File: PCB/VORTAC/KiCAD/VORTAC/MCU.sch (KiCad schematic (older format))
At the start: 1 part

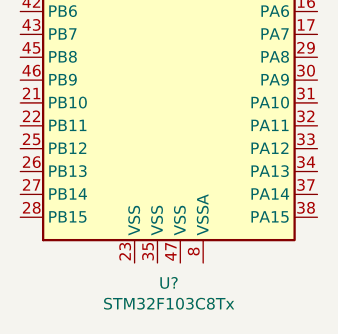
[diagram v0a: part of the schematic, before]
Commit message: pcb, step and headers
-headers schematic updated
-created rough pcb placement of headers
-created step file for inspection in fusion 360
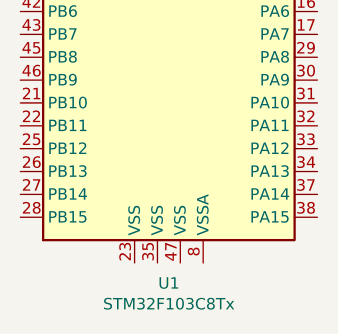
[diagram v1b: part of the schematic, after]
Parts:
- gave numbers to parts that had none: 1
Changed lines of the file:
@@
 $EndDescr
 $Comp
-L MCU_ST_STM32F1:STM32F103C8Tx U?
+L MCU_ST_STM32F1:STM32F103C8Tx U1
 U 1 1 6140AA25
 P 3450 3900
-F 0 "U?" H 3400 2311 50  0000 C CNN
+F 0 "U1" H 3400 2311 50  0000 C CNN
 F 1 "STM32F103C8Tx" H 3400 2220 50  0000 C CNN
 F 2 "Package_QFP:LQFP-48_7x7mm_P0.5mm" H 2850 2500 50  0001 R CNN

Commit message: Schematic and Lib Updates
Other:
- moved on the sheet: U1
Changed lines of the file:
@@
 L MCU_ST_STM32F1:STM32F103C8Tx U1
 U 1 1 6140AA25
-P 3450 3900
-F 0 "U1" H 3400 2311 50  0000 C CNN
-F 1 "STM32F103C8Tx" H 3400 2220 50  0000 C CNN
-F 2 "Package_QFP:LQFP-48_7x7mm_P0.5mm" H 2850 2500 50  0001 R CNN
-F 3 "http://www.st.com/st-web-ui/static/active/en/resource/technical/document/datasheet/CD00161566.pdf" H 3450 3900 50  0001 C CNN
-	1    3450 3900
+P 3500 3550
+F 0 "U1" H 3450 1961 50  0000 C CNN
+F 1 "STM32F103C8Tx" H 3450 1870 50  0000 C CNN
+F 2 "Package_QFP:LQFP-48_7x7mm_P0.5mm" H 2900 2150 50  0001 R CNN
+F 3 "http://www.st.com/st-web-ui/static/active/en/resource/technical/document/datasheet/CD00161566.pdf" H 3500 3550 50  0001 C CNN
+	1    3500 3550
 	1    0    0    -1
 $EndComp

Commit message: pushie
updates and stuff
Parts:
- added 10uH1, 10uH2: L, Inductor_SMD:L_Sunlord_MWSA0518_5.4x5.2mm, symbol Device:L
- added C11, C12: 10uF, Capacitor_SMD:C_1206_3216Metric, symbol Device:C_Small
- added C13, C14, C15, C17: 0.1uF, Capacitor_SMD:C_0603_1608Metric, symbol Device:C_Small
- added C16: 360pF, Capacitor_SMD:C_0603_1608Metric, symbol Device:C_Small
- added C18: 3.3nF, Capacitor_SMD:C_0603_1608Metric, symbol Device:C_Small
- added C19: 30pF, Capacitor_SMD:C_0603_1608Metric, symbol Device:C_Small
- added C20: 56pF, Capacitor_SMD:C_0603_1608Metric, symbol Device:C_Small
- added C21, C23, C25: 47uF, Capacitor_SMD:C_1206_3216Metric, symbol Device:C_Small
- added C22, C24, C26: 47uF, Capacitor_SMD:C_0805_2012Metric, symbol Device:C_Small
- added C? (x2): 1uF, Capacitor_SMD:C_0603_1608Metric, symbol Device:C_Small
- added R28: 36.5k, Resistor_SMD:R_0402_1005Metric, symbol Device:R_Small
- added R29: 10k, Resistor_SMD:R_0402_1005Metric, symbol Device:R_Small
- added R30, R31: 95k, Resistor_SMD:R_0402_1005Metric, symbol Device:R_Small
- added R32, R34: 100k, Resistor_SMD:R_0402_1005Metric, symbol Device:R_Small
- added R33: 7.15k, Resistor_SMD:R_0402_1005Metric, symbol Device:R_Small
- added R35: 19.1k, Resistor_SMD:R_0402_1005Metric, symbol Device:R_Small
- added U3, U4: TPS54335ADRCR, Package_SON:VSON-10-1EP_3x3mm_P0.5mm_EP1.65x2.4mm_ThermalVias, symbol ToolChanger:TPS54335ADRCR
- added U?: TLV73333PDBV, Package_TO_SOT_SMD:SOT-23-5, symbol Regulator_Linear:TLV73333PDBV
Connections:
- new net: R30.2, U3.10 (RT)
- new net: 10uH1.1, C15.1, U3.2 (PH)
- new net: R32.2, R33.1, U3.6 (VSENSE)
- new net: C16.1, R28.2, U3.7 (COMP)
- new net: C15.2, U3.9 (BOOT)
- new net: C19.1, R28.1
- new net: R31.2, U4.10 (RT)
- new net: 10uH2.1, C17.1, U4.2 (PH)
- new net: C17.2, U4.9 (BOOT)
- new net: C20.1, R29.1
- new net: C18.1, R29.2, U4.7 (COMP)
- new net: R34.2, R35.1, U4.6 (VSENSE)
- new net 12V: 10uH1.2, C21.1, C23.1, C25.1, R32.1
- new net 3.3V: C?.1, U?.5 (OUT)
- new net 5V: 10uH2.2, C22.1, C24.1, C26.1, C?.1, R34.1, U?.1 (IN), U?.3 (EN)
- new net GND: C11.2, C12.2, C13.2, C14.2, C16.2, C18.2, C19.2, C20.2, C21.2, C22.2, C23.2, C24.2, C25.2, C26.2, C?.2, C?.2, R30.1, R31.1, R33.2, R35.2, U3.11 (THRM), U3.3 (GND), U3.4 (GND), U3.5 (GND), U4.11 (THRM), U4.3 (GND), U4.4 (GND), U4.5 (GND), U?.2 (GND)
- new net V_IN: C11.1, C12.1, C13.1, C14.1, U3.1 (VIN), U4.1 (VIN)
- no-connect marks 0 -> 2
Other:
- note added: "12V DC-DC Converter\n(capable of min 2A)"
- note added: "5V DC-DC Converter\n(capable of min 2.5A)"
- note added: "R2 = 0.8 / (VOUT-0.8) * 100K\nR2 = 19.047 >> 19.1K\n\nVOUT = 0.8 * R1/R2 + 0.8\nVOUT = 4.98V\n\nRT = 55300/FSW^-1.025\nRT(500 kHz) = 94.68K"
- note added: "R2 = 0.8 / (VOUT-0.8) * 100K\nR2 = 7.142 >> 7.15K\n\nVOUT = 0.8 * R1/R2 + 0.8\nVOUT =11.98V\n\nRT = 55300/FSW^-1.025\nRT(500 kHz) = 94.68K"
- moved on the sheet: U1

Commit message: progress
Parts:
- removed 10uH1, 10uH2: L, Inductor_SMD:L_Sunlord_MWSA0518_5.4x5.2mm, symbol Device:L
- removed C11, C12: 10uF, Capacitor_SMD:C_1206_3216Metric, symbol Device:C_Small
- removed C13, C14, C15, C17: 0.1uF, Capacitor_SMD:C_0603_1608Metric, symbol Device:C_Small
- removed C16: 360pF, Capacitor_SMD:C_0603_1608Metric, symbol Device:C_Small
- removed C18: 3.3nF, Capacitor_SMD:C_0603_1608Metric, symbol Device:C_Small
- removed C19: 30pF, Capacitor_SMD:C_0603_1608Metric, symbol Device:C_Small
- removed C20: 56pF, Capacitor_SMD:C_0603_1608Metric, symbol Device:C_Small
- removed C? (x2): 1uF, Capacitor_SMD:C_0603_1608Metric, symbol Device:C_Small
- removed R28: 36.5k, Resistor_SMD:R_0402_1005Metric, symbol Device:R_Small
- removed R29: 10k, Resistor_SMD:R_0402_1005Metric, symbol Device:R_Small
- removed U3, U4: TPS54335ADRCR, Package_SON:VSON-10-1EP_3x3mm_P0.5mm_EP1.65x2.4mm_ThermalVias, symbol ToolChanger:TPS54335ADRCR
- removed U?: TLV73333PDBV, Package_TO_SOT_SMD:SOT-23-5, symbol Regulator_Linear:TLV73333PDBV
- added C27, C28, C30: 470pF 100V, Capacitor_SMD:C_0603_1608Metric, symbol Device:C_Small
- added C29: 0.1uF 50V, Capacitor_SMD:C_0603_1608Metric, symbol Device:C_Small
- added C31, C33: 100nF 16V, Capacitor_SMD:C_0603_1608Metric, symbol Device:C_Small
- added C32: C_Small, symbol Device:C_Small
- added C34: 100uF 35V, Capacitor_SMD:CP_Elec_8x6.9, symbol Device:CP
- added IC1: TMC2209-LA, ToolChanger:tmc_2209_package, symbol ToolChanger:TMC2209-LA
- added R36: 22R, Resistor_SMD:R_0402_1005Metric, symbol Device:R_Small
- added U5: ADXL345BCCZ-RL7, Package_LGA:LGA-14_3x5mm_P0.8mm_LayoutBorder1x6y, symbol Sensor_Motion:ADXL343
- C21: value 47uF -> 0.1uF 50V; footprint Capacitor_SMD:C_1206_3216Metric -> Capacitor_SMD:C_0603_1608Metric; LCSC C403725 -> (none)
- C22, C24, C26: value 47uF -> 0.1uF 50V; footprint Capacitor_SMD:C_0805_2012Metric -> Capacitor_SMD:C_0603_1608Metric; LCSC C466799 -> (none)
- C23: value 47uF -> 22nF X7R 10% 50V; footprint Capacitor_SMD:C_1206_3216Metric -> Capacitor_SMD:C_0603_1608Metric; LCSC C403725 -> (none)
- C25: value 47uF -> 470pF 100V; footprint Capacitor_SMD:C_1206_3216Metric -> Capacitor_SMD:C_0603_1608Metric; LCSC C403725 -> C437459
- R30: value 95k -> 0.1R 1%; footprint Resistor_SMD:R_0402_1005Metric -> Resistor_SMD:R_1206_3216Metric; LCSC (none) -> C346768
- R31: value 95k -> 1K; footprint Resistor_SMD:R_0402_1005Metric -> (none)
- R32: value 100k -> 22K
- R33: value 7.15k -> 22K
- R34: value 100k -> 0.1R 1%; footprint Resistor_SMD:R_0402_1005Metric -> Resistor_SMD:R_1206_3216Metric; LCSC (none) -> C346768
- R35: value 19.1k -> 22R
- renumbered U1 to U2
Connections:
- net 3.3V: now also C21.1, R32.2, IC1.15 (VCC_IO)
- net GND: now also C25.1, C26.1, R34.1, C27.1, C28.1, C29.1, C30.1, C31.1, C32.2, C33.1, C34.2, IC1.10 (MS2_AD1), IC1.13 (CLK), IC1.18 (GND), IC1.20 (STDBY), IC1.29 (GNDPAD), IC1.3 (GND), IC1.7 (SPREAD), IC1.9 (MS1_AD0), U5.2 (GND), U5.4 (GND), U5.5 (GND); no longer C23.2, C24.2, C25.2, C26.2, R31.1, R35.2
- net V_IN: now also C24.2, C26.2, C29.2, C34.1, IC1.22 (VS), IC1.28 (VS)
- net USART_2_TX: now reaches U2.12 (PA2)
- net USART_2_RX: now reaches U2.13 (PA3)
- net USART_3_TX: now reaches U2.21 (PB10)
- net USART_3_RX: now reaches U2.22 (PB11)
- net USART_1_TX: now reaches U2.30 (PA9)
- net USART_1_RX: now reaches U2.31 (PA10)
- net at U2.32 (PA11): now also R35.2
- net at U2.33 (PA12): now also R36.2
- net CAN_RX: now reaches U2.45 (PB8)
- net CAN_TX: now reaches U2.46 (PB9)
- net TMC_BRB: now reaches R30.2
- net TMC_BRB: now also C31.2, IC1.27 (BRB)
- net TMC_UART_RX: now reaches R33.1
- net TMC_UART_RX: now also R31.2, IC1.14 (PDN_UART); no longer R32.2
- net TMC_BRA: now reaches R34.2
- net TMC_BRA: now also C33.2, IC1.23 (BRA); no longer R35.1
- removed net 12V: C21.1, C23.1, C25.1, R32.1
- removed net 5V: C22.1, C24.1, C26.1, R34.1
- new net: C23.1, IC1.5 (CPI)
- new net: C23.2, IC1.4 (CPO)
- new net: C24.1, IC1.6 (VCP)
- new net: C22.1, IC1.8 (5VOUT)
- new net ADXL_AREF: C32.1, U5.1 (Vdd_I/O), U5.6 (Vs)
- new net ADXL_CS: U5.7 (~CS)
- new net ADXL_INT1: U5.8 (INT1)
- new net ADXL_SCL: U5.14 (SCL/SCLK)
- new net ADXL_SDI: U5.13 (SDA/SDI/SDIO)
- new net ADXL_SDO: U5.12 (SDO/ADDR)
- new net STEP_1_A1: C28.2, IC1.24 (OA1)
- new net STEP_1_A2: C30.2, IC1.21 (OA2)
- new net STEP_1_B1: C27.2, IC1.26 (OB1)
- new net STEP_1_B2: C25.2, IC1.1 (OB2)
- new net TMC_DIAG: IC1.11 (DIAG)
- new net TMC_DIR: IC1.19 (DIR)
- new net TMC_ENN: IC1.2 (ENN), R32.1
- new net TMC_STEP: IC1.16 (STEP)
- new net TMC_UART_TX: R31.1
- new net USB_D+: R36.1
- new net USB_D-: R35.1
- no-connect marks 2 -> 5
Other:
- note added: "0.1R shunts to allow max stepper current of 2A\n0.22R shunts for <1A but improved low current accuracy\nTODO: change to 0.22R for grabber"
- note added: "470pF caps on stepper coils as simple esd protection\n100nF caps on sense resistors as simple esd protection\nTODO: consider grounding stepper motor"
- note added: "ADXL_345"
- note added: "Integrated Stepper Driver"
- note removed: "12V DC-DC Converter\n(capable of min 2A)"
- note removed: "5V DC-DC Converter\n(capable of min 2.5A)"
- note removed: "R2 = 0.8 / (VOUT-0.8) * 100K\nR2 = 19.047 >> 19.1K\n\nVOUT = 0.8 * R1/R2 + 0.8\nVOUT = 4.98V\n\nRT = 55300/FSW^-1.025\nRT(500 kHz) = 94.68K"
- note removed: "R2 = 0.8 / (VOUT-0.8) * 100K\nR2 = 7.142 >> 7.15K\n\nVOUT = 0.8 * R1/R2 + 0.8\nVOUT =11.98V\n\nRT = 55300/FSW^-1.025\nRT(500 kHz) = 94.68K"
- moved on the sheet: U2

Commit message: progress
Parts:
- added C?: C_Small, Capacitor_SMD:C_0402_1005Metric, symbol Device:C_Small
- added U6: TJA1040T, Package_SO:SOIC-8_3.9x4.9mm_P1.27mm, symbol ToolChanger:TJA1040T
- C32: footprint (none) -> Capacitor_SMD:C_0402_1005Metric
- R31: footprint (none) -> Resistor_SMD:R_0402_1005Metric
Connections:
- net labels added: CAN_H, CAN_L
- wire segments 107 -> 120
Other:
- moved on the sheet: R35, R36, U2
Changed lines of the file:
@@
 encoding utf-8
 Sheet 4 4
-Title ""
-Date ""
-Rev ""
-Comp ""
-Comment1 ""
-Comment2 ""
-Comment3 ""
-Comment4 ""
+Title "MCU & ICS"
+Date "2021-10-17"
+Rev "0.0"
+Comp "VORTAC DESIGN"
+Comment1 "!! wip untested revesion !!"
+Comment2 "Designed to be used with Klipper Firmware"
+Comment3 "Canbus Networked Smart Tool Board"
+Comment4 "-- VORTAC PCB --"
 $EndDescr
 $Comp
 L MCU_ST_STM32F1:STM32F103C8Tx U2
 U 1 1 6140AA25
-P 2500 2800
-F 0 "U2" H 2450 1211 50  0000 C CNN
-F 1 "STM32F103C8Tx" H 2450 1120 50  0000 C CNN
-F 2 "Package_QFP:LQFP-48_7x7mm_P0.5mm" H 1900 1400 50  0001 R CNN
-F 3 "http://www.st.com/st-web-ui/static/active/en/resource/technical/document/datasheet/CD00161566.pdf" H 2500 2800 50  0001 C CNN
-	1    2500 2800
+P 3000 2550
+F 0 "U2" H 2950 961 50  0000 C CNN
+F 1 "STM32F103C8Tx" H 2950 870 50  0000 C CNN
+F 2 "Package_QFP:LQFP-48_7x7mm_P0.5mm" H 2400 1150 50  0001 R CNN
+F 3 "http://www.st.com/st-web-ui/static/active/en/resource/technical/document/datasheet/CD00161566.pdf" H 3000 2550 50  0001 C CNN
+	1    3000 2550
 	1    0    0    -1
 $EndComp
@@
 F 0 "C32" H 10292 5196 50  0000 L CNN
 F 1 "C_Small" H 10292 5105 50  0000 L CNN
-F 2 "" H 10200 5150 50  0001 C CNN
+F 2 "Capacitor_SMD:C_0402_1005Metric" H 10200 5150 50  0001 C CNN
 F 3 "~" H 10200 5150 50  0001 C CNN
 	1    10200 5150
@@
 F 0 "R31" V 6550 2050 50  0000 L CNN
 F 1 "1K" V 6650 2050 50  0000 L CNN
-F 2 "" H 6750 2100 50  0001 C CNN
+F 2 "Resistor_SMD:R_0402_1005Metric" H 6750 2100 50  0001 C CNN
 F 3 "~" H 6750 2100 50  0001 C CNN
 	1    6750 2100
@@
 L Device:R_Small R?
 U 1 1 61C61B07
-P 3400 3700
+P 3900 3450
 AR Path="/613DB78D/61C61B07" Ref="R?"  Part="1"
 AR Path="/613DC005/61C61B07" Ref="R35"  Part="1"
-F 0 "R35" V 3400 3700 50  0000 C CNN
-F 1 "22R" V 3350 3850 50  0000 C CNN
-F 2 "Resistor_SMD:R_0402_1005Metric" V 3330 3700 50  0001 C CNN
-F 3 "~" H 3400 3700 50  0001 C CNN
-	1    3400 3700
+F 0 "R35" V 3900 3450 50  0000 C CNN
+F 1 "22R" V 3850 3600 50  0000 C CNN
+F 2 "Resistor_SMD:R_0402_1005Metric" V 3830 3450 50  0001 C CNN
+F 3 "~" H 3900 3450 50  0001 C CNN
+	1    3900 3450
 	0    1    1    0
 $EndComp
@@
 L Device:R_Small R?
 U 1 1 61C61B0D
-P 3550 3800
+P 4050 3550
 AR Path="/613DB78D/61C61B0D" Ref="R?"  Part="1"
 AR Path="/613DC005/61C61B0D" Ref="R36"  Part="1"
-F 0 "R36" V 3550 3800 50  0000 C CNN
-F 1 "22R" V 3500 3950 50  0000 C CNN
-F 2 "Resistor_SMD:R_0402_1005Metric" V 3480 3800 50  0001 C CNN
-F 3 "~" H 3550 3800 50  0001 C CNN
-	1    3550 3800
+F 0 "R36" V 4050 3550 50  0000 C CNN
+F 1 "22R" V 4000 3700 50  0000 C CNN
+F 2 "Resistor_SMD:R_0402_1005Metric" V 3980 3550 50  0001 C CNN
+F 3 "~" H 4050 3550 50  0001 C CNN
+	1    4050 3550
 	0    1    1    0
 $EndComp
-Text GLabel 3850 3800 2    50   Input ~ 0
+Text GLabel 4350 3550 2    50   Input ~ 0
 USB_D+
-Text GLabel 3850 3700 2    50   Input ~ 0
+Text GLabel 4350 3450 2    50   Input ~ 0
 USB_D-
 Wire Wire Line
-	3650 3800 3850 3800
-Text GLabel 1600 3500 0    50   Input ~ 0
+	4150 3550 4350 3550
+Text GLabel 2100 3250 0    50   Input ~ 0
 CAN_TX
-Text GLabel 1600 3400 0    50   Input ~ 0
+Text GLabel 2100 3150 0    50   Input ~ 0
 CAN_RX
 Wire Wire Line
-	1600 3400 1800 3400
-Wire Wire Line
-	1600 3500 1800 3500
-Text GLabel 3850 3500 2    50   Input ~ 0
+	2100 3150 2300 3150
+Wire Wire Line
+	2100 3250 2300 3250
+Text GLabel 4350 3250 2    50   Input ~ 0
 USART_1_TX
-Text GLabel 3850 3600 2    50   Input ~ 0
+Text GLabel 4350 3350 2    50   Input ~ 0
 USART_1_RX
 Wire Wire Line
-	3100 3700 3300 3700
-Wire Wire Line
-	3500 3700 3850 3700
-Wire Wire Line
-	3100 3600 3850 3600
-Wire Wire Line
-	3100 3500 3850 3500
-Wire Wire Line
-	3100 3800 3450 3800
-Text GLabel 1600 3600 0    50   Input ~ 0
+	3600 3450 3800 3450
+Wire Wire Line
+	4000 3450 4350 3450
+Wire Wire Line
+	3600 3350 4350 3350
+Wire Wire Line
+	3600 3250 4350 3250
+Wire Wire Line
+	3600 3550 3950 3550
+Text GLabel 2100 3350 0    50   Input ~ 0
 USART_3_TX
-Text GLabel 1600 3700 0    50   Input ~ 0
+Text GLabel 2100 3450 0    50   Input ~ 0
 USART_3_RX
 Wire Wire Line
-	1600 3600 1800 3600
-Wire Wire Line
-	1600 3700 1800 3700
-Text GLabel 3350 2800 2    50   Input ~ 0
+	2100 3350 2300 3350
+Wire Wire Line
+	2100 3450 2300 3450
+Text GLabel 3850 2550 2    50   Input ~ 0
 USART_2_TX
-Text GLabel 3350 2900 2    50   Input ~ 0
+Text GLabel 3850 2650 2    50   Input ~ 0
 USART_2_RX
 Wire Wire Line
-	3100 2800 3350 2800
-Wire Wire Line
-	3100 2900 3350 2900
+	3600 2550 3850 2550
+Wire Wire Line
+	3600 2650 3850 2650
+$Comp
+L ToolChanger:TJA1040T U6
+U 1 1 619288F5
+P 6900 5400
+F 0 "U6" H 6400 6000 50  0000 C CNN
+F 1 "TJA1040T" H 6500 5850 50  0000 C CNN
+F 2 "Package_SO:SOIC-8_3.9x4.9mm_P1.27mm" H 6900 4900 50  0001 C CIN
+F 3 "http://www.nxp.com/documents/data_sheet/TJA1049.pdf" H 6900 5400 50  0001 C CNN
+	1    6900 5400
+	1    0    0    -1
+$EndComp
+Wire Wire Line
+	6750 5800 6750 5900
+Wire Wire Line
+	6750 5900 6900 5900
+Wire Wire Line
+	6900 5900 6900 5800
+Wire Wire Line
+	6900 5900 7050 5900
+Wire Wire Line
+	7050 5900 7050 5800
+Connection ~ 6900 5900
+Wire Wire Line
+	7050 5900 7050 6000
+Connection ~ 7050 5900
+$Comp
+L power:GND #PWR?
+U 1 1 6194692B
+P 7050 6000
+AR Path="/613DBE83/6194692B" Ref="#PWR?"  Part="1"
+AR Path="/613DC005/6194692B" Ref="#PWR0121"  Part="1"
+F 0 "#PWR0121" H 7050 5750 50  0001 C CNN
+F 1 "GND" H 7055 5827 50  0000 C CNN
+F 2 "" H 7050 6000 50  0001 C CNN
+F 3 "" H 7050 6000 50  0001 C CNN
+	1    7050 6000
+	1    0    0    -1
+$EndComp
+Text GLabel 7600 4900 2    50   Input ~ 0
+3.3V
+Text GLabel 7600 5350 2    50   Input ~ 0
+CAN_H
+Text GLabel 7600 5450 2    50   Input ~ 0
+CAN_L
+Wire Wire Line
+	7400 5350 7600 5350
+Wire Wire Line
+	7400 5450 7600 5450
+Wire Wire Line
+	6400 5350 6200 5350
+Text GLabel 6200 5350 0    50   Input ~ 0
+CAN_TX
+Text GLabel 6200 5450 0    50   Input ~ 0
+CAN_RX
+Wire Wire Line
+	6200 5450 6400 5450
+$Comp
+L power:GND #PWR?
+U 1 1 619A4E4A
+P 7500 5200
+AR Path="/613DBE83/619A4E4A" Ref="#PWR?"  Part="1"
+AR Path="/613DC005/619A4E4A" Ref="#PWR?"  Part="1"
+F 0 "#PWR?" H 7500 4950 50  0001 C CNN
+F 1 "GND" H 7650 5150 50  0000 C CNN
+F 2 "" H 7500 5200 50  0001 C CNN
+F 3 "" H 7500 5200 50  0001 C CNN
+	1    7500 5200
+	1    0    0    -1
+$EndComp
+$Comp
+L Device:C_Small C?
+U 1 1 619A4E50
+P 7500 5100
+AR Path="/613DBE83/619A4E50" Ref="C?"  Part="1"
+AR Path="/613DC005/619A4E50" Ref="C?"  Part="1"
+F 0 "C?" H 7592 5146 50  0000 L CNN
+F 1 "C_Small" H 7592 5055 50  0000 L CNN
+F 2 "Capacitor_SMD:C_0402_1005Metric" H 7500 5100 50  0001 C CNN
+F 3 "~" H 7500 5100 50  0001 C CNN
+	1    7500 5100
+	1    0    0    -1
+$EndComp
+Wire Wire Line
+	6900 4900 7500 4900
+Wire Wire Line
+	7500 4900 7500 5000
+Connection ~ 7500 4900
+Wire Wire Line
+	7500 4900 7600 4900
 $EndSCHEMATC

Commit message: Layouting & Footprints
-Improved Thermal Footprint Conductivity
-Improved Component Spacing
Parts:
- IC1: footprint ToolChanger:tmc_2209_package -> ToolChanger:tmc_2209_VORTAC
- U6: footprint Package_SO:SOIC-8_3.9x4.9mm_P1.27mm -> ToolChanger:SOIC-8_3.9x4.9mm_P1.27mm
- gave numbers to parts that had none: 1
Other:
- note added: "todo \n-consider AREF implementation\n-3.3v vs AREF for ADXL & CAN\n\n>> routing for can therm and can gets kinda awkward\n>> can and therm should be unified to AREF or 3.3"
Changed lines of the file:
@@
 F 0 "IC1" H 8250 3350 50  0000 C CNN
 F 1 "TMC2209-LA" H 8250 3250 50  0000 C CNN
-F 2 "ToolChanger:tmc_2209_package" V 8350 1550 50  0001 L CNN
+F 2 "ToolChanger:tmc_2209_VORTAC" V 8350 1550 50  0001 L CNN
 F 3 "https://www.lcsc.com/product-detail/Motor-Driver-ICs_TRINAMIC-Motion-Control-GmbH-TMC2209-LA_C465949.html" H 7200 2900 50  0001 L CNN
 F 4 "C465949" V 8250 2500 50  0001 C CNN "LCSC"
@@
 F 0 "U6" H 6400 6000 50  0000 C CNN
 F 1 "TJA1040T" H 6500 5850 50  0000 C CNN
-F 2 "Package_SO:SOIC-8_3.9x4.9mm_P1.27mm" H 6900 4900 50  0001 C CIN
+F 2 "ToolChanger:SOIC-8_3.9x4.9mm_P1.27mm" H 6900 4900 50  0001 C CIN
 F 3 "http://www.nxp.com/documents/data_sheet/TJA1049.pdf" H 6900 5400 50  0001 C CNN
 	1    6900 5400
@@
 P 7500 5200
 AR Path="/613DBE83/619A4E4A" Ref="#PWR?"  Part="1"
-AR Path="/613DC005/619A4E4A" Ref="#PWR?"  Part="1"
-F 0 "#PWR?" H 7500 4950 50  0001 C CNN
+AR Path="/613DC005/619A4E4A" Ref="#PWR0122"  Part="1"
+F 0 "#PWR0122" H 7500 4950 50  0001 C CNN
 F 1 "GND" H 7650 5150 50  0000 C CNN
 F 2 "" H 7500 5200 50  0001 C CNN
@@
 P 7500 5100
 AR Path="/613DBE83/619A4E50" Ref="C?"  Part="1"
-AR Path="/613DC005/619A4E50" Ref="C?"  Part="1"
-F 0 "C?" H 7592 5146 50  0000 L CNN
+AR Path="/613DC005/619A4E50" Ref="C35"  Part="1"
+F 0 "C35" H 7592 5146 50  0000 L CNN
 F 1 "C_Small" H 7592 5055 50  0000 L CNN
 F 2 "Capacitor_SMD:C_0402_1005Metric" H 7500 5100 50  0001 C CNN
@@
 Wire Wire Line
 	7500 4900 7600 4900
+Text Notes 4500 6250 0    50   ~ 0
+todo \n-consider AREF implementation\n-3.3v vs AREF for ADXL & CAN\n\n>> routing for can therm and can gets kinda awkward\n>> can and therm should be unified to AREF or 3.3
 $EndSCHEMATC

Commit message: IT l0oks like a Face FML =/
thanks henny
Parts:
- IC1: footprint ToolChanger:tmc_2209_VORTAC -> ToolChanger:tmc_2209_package
- U2: LCSC (none) -> C8734
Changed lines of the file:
@@
 F 1 "STM32F103C8Tx" H 2950 870 50  0000 C CNN
 F 2 "Package_QFP:LQFP-48_7x7mm_P0.5mm" H 2400 1150 50  0001 R CNN
-F 3 "http://www.st.com/st-web-ui/static/active/en/resource/technical/document/datasheet/CD00161566.pdf" H 3000 2550 50  0001 C CNN
+F 3 "http://www.st.com/st-web-https://www.lcsc.com/product-detail/ST-Microelectronics_STMicroelectronics-STM32F103C8T6_C8734.html" H 3000 2550 50  0001 C CNN
+F 4 "C8734" H 3000 2550 50  0001 C CNN "LCSC"
 	1    3000 2550
 	1    0    0    -1
@@
 F 0 "IC1" H 8250 3350 50  0000 C CNN
 F 1 "TMC2209-LA" H 8250 3250 50  0000 C CNN
-F 2 "ToolChanger:tmc_2209_VORTAC" V 8350 1550 50  0001 L CNN
+F 2 "ToolChanger:tmc_2209_package" V 8350 1550 50  0001 L CNN
 F 3 "https://www.lcsc.com/product-detail/Motor-Driver-ICs_TRINAMIC-Motion-Control-GmbH-TMC2209-LA_C465949.html" H 7200 2900 50  0001 L CNN
 F 4 "C465949" V 8250 2500 50  0001 C CNN "LCSC"

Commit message: Routing WIP
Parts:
- added C36, C37, C38, C39: 0.1uF 16V, Capacitor_SMD:C_0402_1005Metric, symbol Device:C_Small
- added C40: 4.7uF 10V, Capacitor_SMD:C_0402_1005Metric, symbol Device:C_Small
- added C41: 0.1uF 16V, Capacitor_SMD:C_0603_1608Metric, symbol Device:C_Small
- added C42, C43: C_Small, Capacitor_SMD:C_0402_1005Metric, symbol Device:C_Small
- added C44: 10nF, Capacitor_SMD:C_0402_1005Metric, symbol Device:C_Small
- added C45: 1uF, Capacitor_SMD:C_0402_1005Metric, symbol Device:C_Small
- added D6: LED_Small, symbol Device:LED_Small
- added HSE1: 8MHz, Crystal:Crystal_SMD_3225-4Pin_3.2x2.5mm, symbol Device:Crystal_GND24_Small
- added L3: 10uH 15mA, Inductor_SMD:L_0805_2012Metric, symbol Device:L_Small
- added R37: R_Small, Resistor_SMD:R_0402_1005Metric, symbol Device:R_Small
- added R38: R_Small, symbol Device:R_Small
- C21, C22, C24, C26, C29: LCSC (none) -> C1591
- C31: value 100nF 16V -> 0.1uF 16V
- C33: value 100nF 16V -> 0.1uF 16V; footprint Capacitor_SMD:C_0603_1608Metric -> Capacitor_SMD:C_0402_1005Metric; LCSC C66501 -> C1525
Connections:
- net labels added: +3.3V, +3.3VA, BOOT_0, BOOT_1, DEBUG_SWCLK, DEBUG_SWDIO, DEBUG_SWO, FAN_1_GATE, FAN_1_TACHO, FAN_2_GATE, FAN_2_TACHO, HEATER_GATE, HOST_USB_GATE, HSE_OSC_IN, HSE_OSC_OUT, IO_1_OUT, IO_2_OUT, IO_3_OUT, LED_0, LED_1_GATE, NRST, THERM_1_PIN, TOOL_ID, VDC
- net labels removed: 3.3V, ADXL_AREF, V_IN
- wire segments 120 -> 183
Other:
- note added: "!!esd caps could be smaller 0402 vs 0603!!\n!!alternatively these could be changed to \n50V which are already in BOM!!"
- note added: "4.7uF cap must be placed \non VDD3 >> pin48"
- note added: "CANBUS Transiever"
- note added: "Optional Asynchronous SW"
- moved on the sheet: C32, C35, R35, R36, U2, U5
